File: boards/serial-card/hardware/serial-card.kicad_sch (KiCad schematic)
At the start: 62 parts, among them J10 STACK BUS, J11 RACK 12V, J20 RS-232 1, J21 RS-232 2, J30 RS-485 3, J31 RS-485 4, U1 ST3232B, U10 ISOW1432, U11 ISOW1432

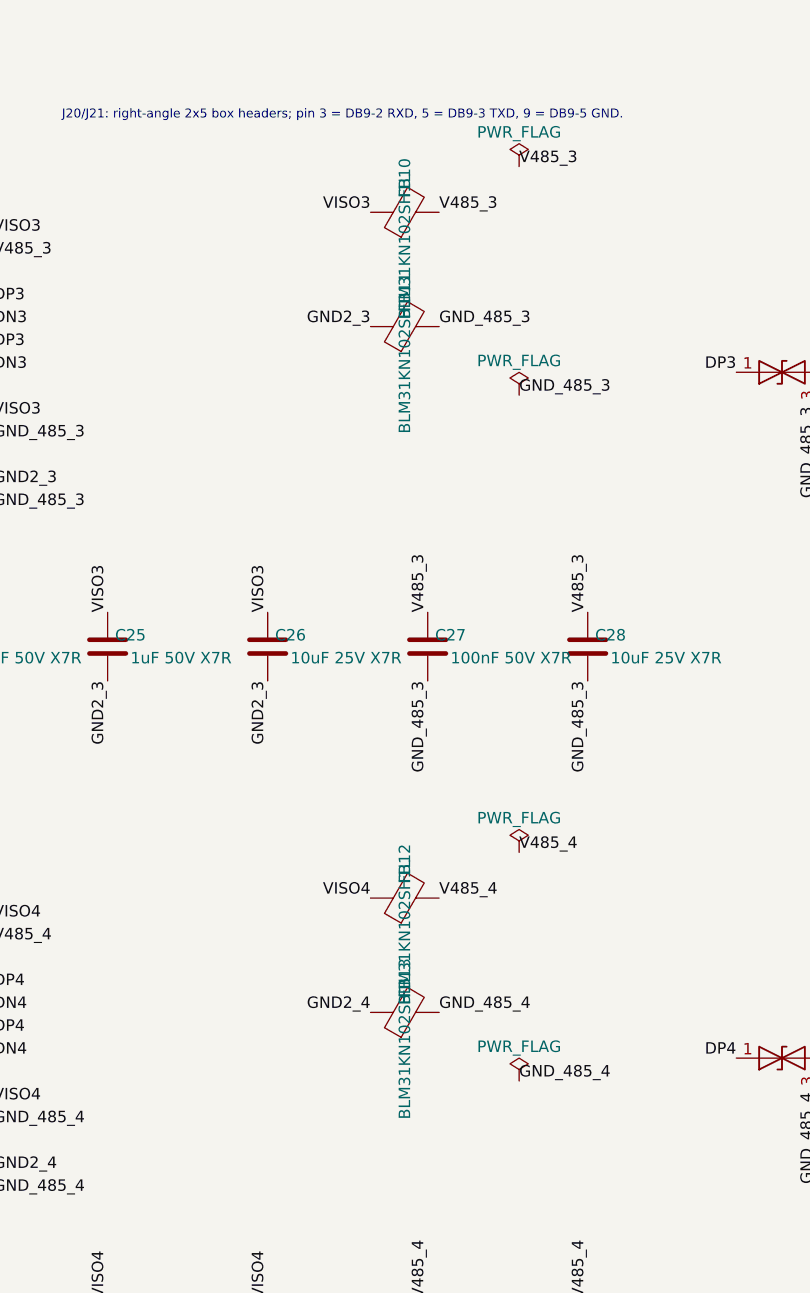
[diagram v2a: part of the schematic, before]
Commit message: Rev B / rev A order: 10 uF CL31B106KAHZW6E, beads BLM31PG391SN1L
Both earlier substitutes (CL31B106KAHNNNE, BLM31KN102SH1L) are on
backorder at Mouser. CL31B106KAHZW6E has the same rating (1.4 mm tall).
The isolated-supply beads need no 1 kOhm: TI's reference uses 330 Ohm;
BLM31PG391SN1L is 390 Ohm @ 100 MHz, 2 A, 50 mOhm. Field-only changes;
order lists regenerated.

Co-Authored-By: Claude Opus 5.5 <noreply@anthropic.com>
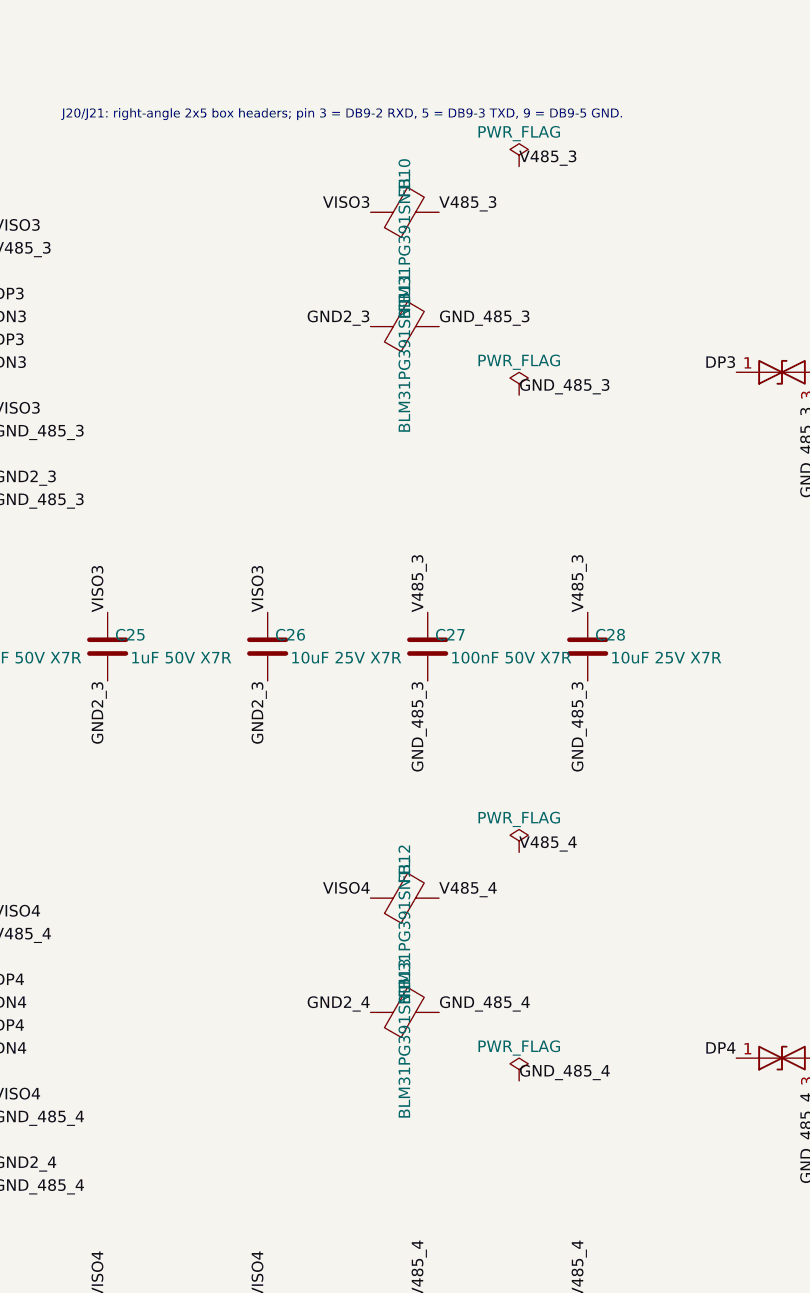
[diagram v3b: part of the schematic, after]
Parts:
- C23, C26, C28, C33, C36, C38, C6, C7: MPN CL31B106KAHNNNE -> CL31B106KAHZW6E
- FB10, FB11, FB12, FB13: value BLM31KN102SH1L -> BLM31PG391SN1L; MPN BLM31KN102SH1L -> BLM31PG391SN1L
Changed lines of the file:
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@@
 			)
 		)
-		(property "MPN" "CL31B106KAHNNNE"
+		(property "MPN" "CL31B106KAHZW6E"
 			(at 104.14 190.5 0)
 			(hide yes)
@@
 			)
 		)
-		(property "MPN" "CL31B106KAHNNNE"
+		(property "MPN" "CL31B106KAHZW6E"
 			(at 162.56 190.5 0)
 			(hide yes)
@@
 			)
 		)
-		(property "Value" "BLM31KN102SH1L"
+		(property "Value" "BLM31PG391SN1L"
 			(at 177.8 146.05 0)
 			(effects
@@
 			)
 		)
-		(property "MPN" "BLM31KN102SH1L"
+		(property "MPN" "BLM31PG391SN1L"
 			(at 177.8 142.24 0)
 			(hide yes)
@@
 			)
 		)
-		(property "Value" "BLM31KN102SH1L"
+		(property "Value" "BLM31PG391SN1L"
 			(at 177.8 158.75 0)
 			(effects
@@
 			)
 		)
-		(property "MPN" "BLM31KN102SH1L"
+		(property "MPN" "BLM31PG391SN1L"
 			(at 177.8 154.94 0)
 			(hide yes)
@@
 			)
 		)
-		(property "MPN" "CL31B106KAHNNNE"
+		(property "MPN" "CL31B106KAHZW6E"
 			(at 198.12 190.5 0)
 			(hide yes)
@@
 			)
 		)
-		(property "MPN" "CL31B106KAHNNNE"
+		(property "MPN" "CL31B106KAHZW6E"
 			(at 104.14 266.7 0)
 			(hide yes)
@@
 			)
 		)
-		(property "MPN" "CL31B106KAHNNNE"
+		(property "MPN" "CL31B106KAHZW6E"
 			(at 162.56 266.7 0)
 			(hide yes)
@@
 			)
 		)
-		(property "Value" "BLM31KN102SH1L"
+		(property "Value" "BLM31PG391SN1L"
 			(at 177.8 222.25 0)
 			(effects
@@
 			)
 		)
-		(property "MPN" "BLM31KN102SH1L"
+		(property "MPN" "BLM31PG391SN1L"
 			(at 177.8 218.44 0)
 			(hide yes)
@@
 			)
 		)
-		(property "Value" "BLM31KN102SH1L"
+		(property "Value" "BLM31PG391SN1L"
 			(at 177.8 234.95 0)
 			(effects
@@
 			)
 		)
-		(property "MPN" "BLM31KN102SH1L"
+		(property "MPN" "BLM31PG391SN1L"
 			(at 177.8 231.14 0)
 			(hide yes)
@@
 			)
 		)
-		(property "MPN" "CL31B106KAHNNNE"
+		(property "MPN" "CL31B106KAHZW6E"
 			(at 198.12 266.7 0)
 			(hide yes)
@@
 			)
 		)
-		(property "MPN" "CL31B106KAHNNNE"
+		(property "MPN" "CL31B106KAHZW6E"
 			(at 342.9 190.5 0)
 			(hide yes)
@@
 			)
 		)
-		(property "MPN" "CL31B106KAHNNNE"
+		(property "MPN" "CL31B106KAHZW6E"
 			(at 363.22 190.5 0)
 			(hide yes)
